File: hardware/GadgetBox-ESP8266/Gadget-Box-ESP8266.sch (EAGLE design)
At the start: 31 parts, among them U1 MCP73831T-2ACI/OT, U2 AP2112-3.3

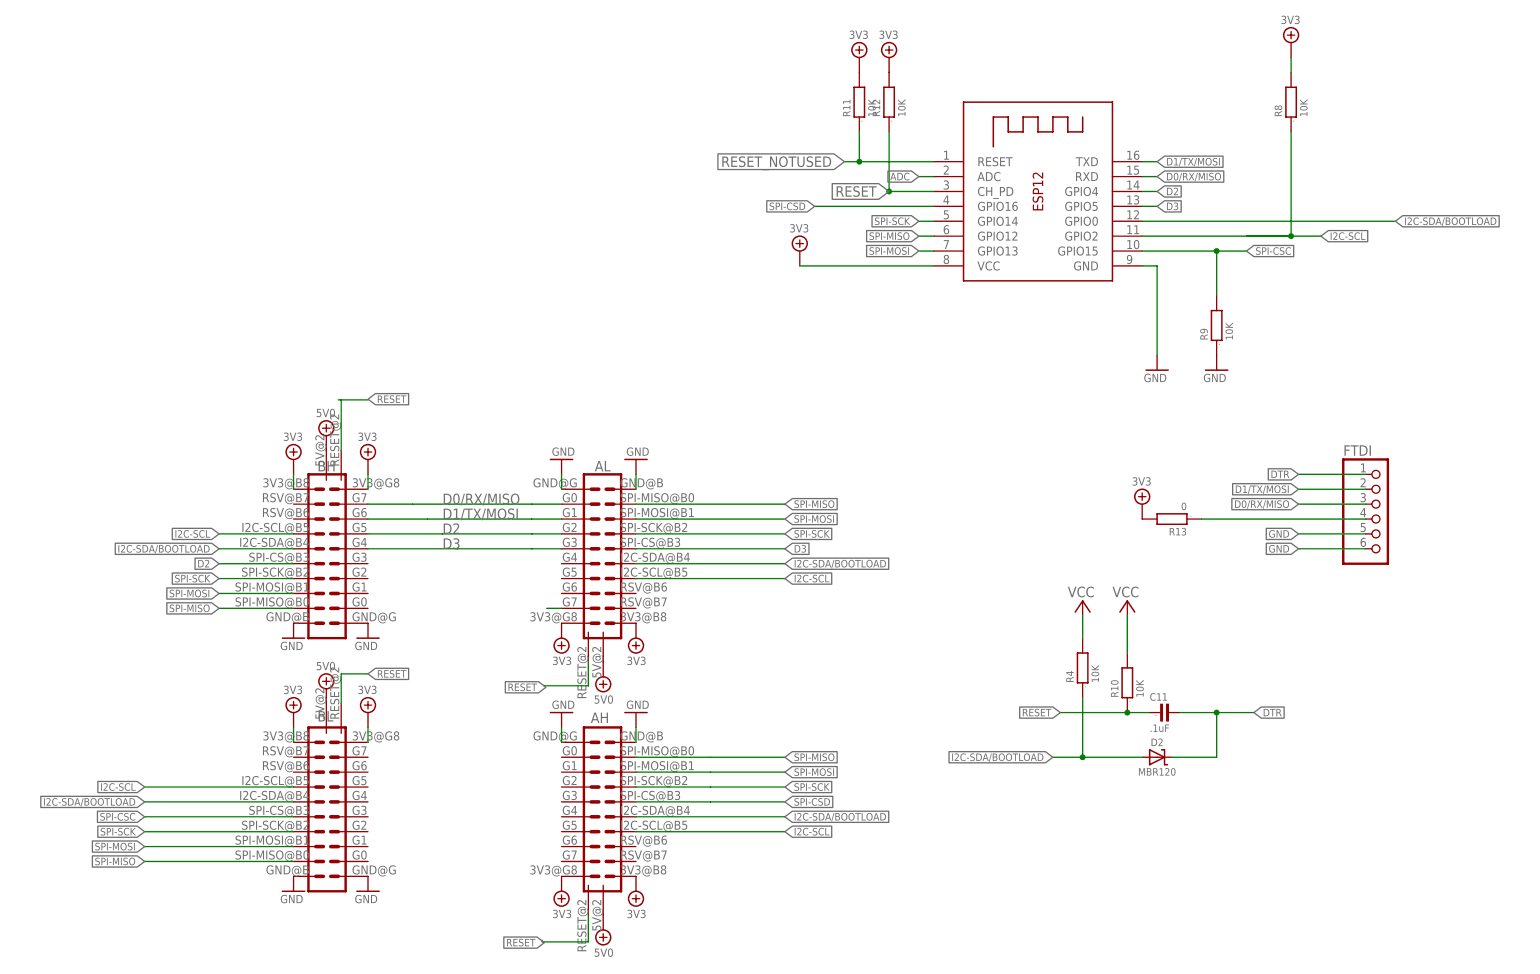
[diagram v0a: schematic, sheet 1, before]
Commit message: Removed Alt eCog headers and re-routed outside traces.
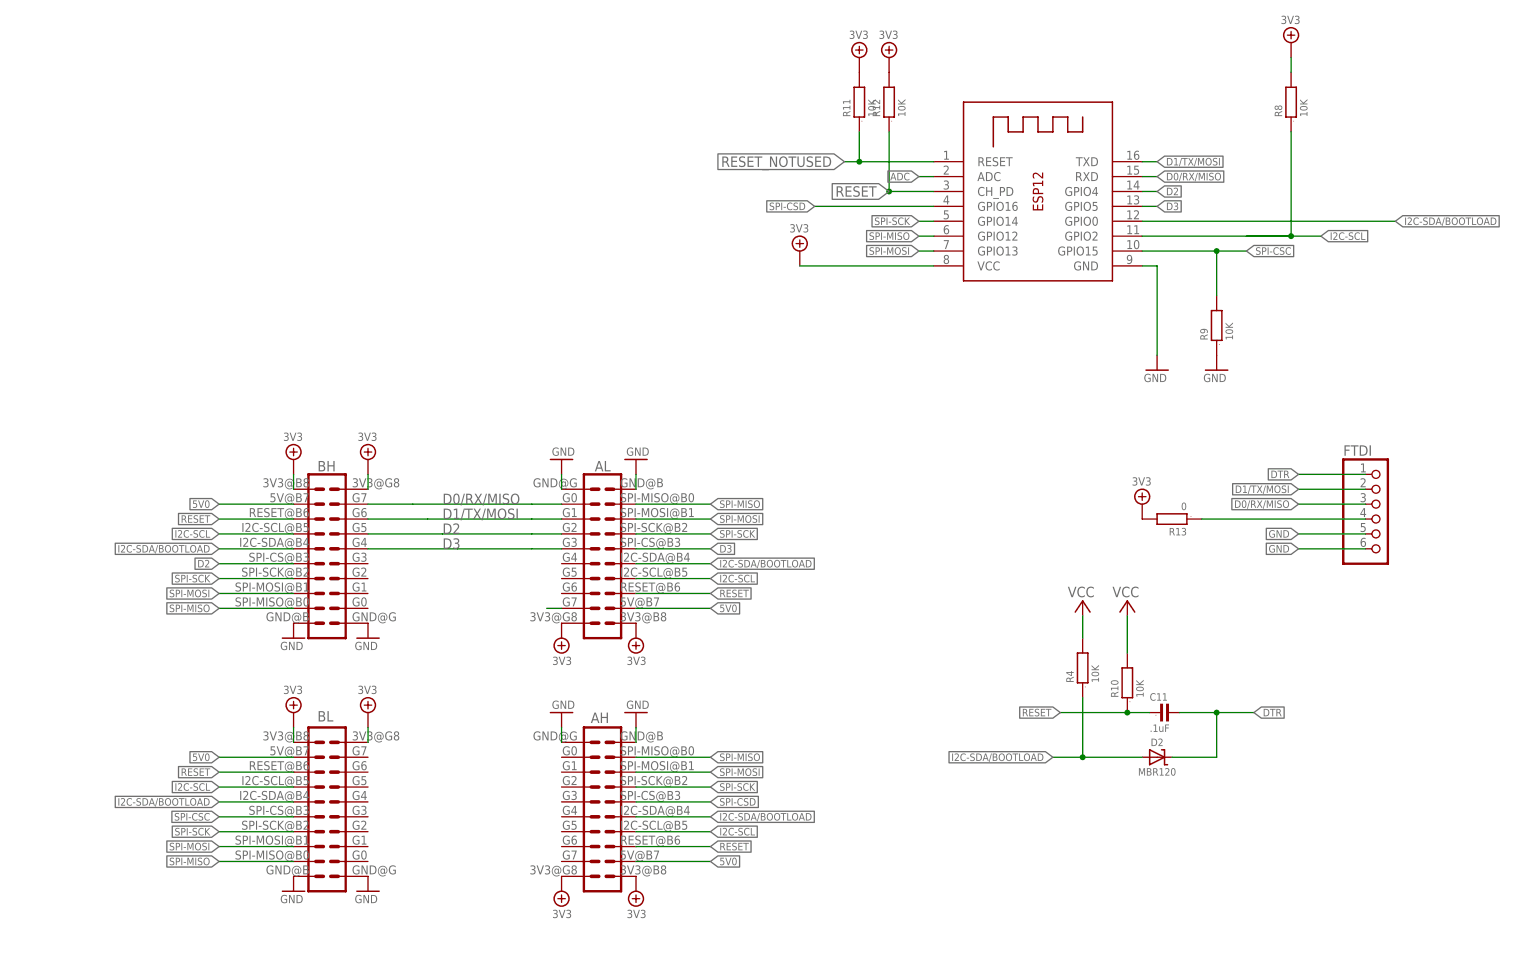
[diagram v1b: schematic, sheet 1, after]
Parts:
- AH, AL, BH, BL: value ECOGECOG_SLOT_ALT1 -> ECOGECOG_SLOT; device eCogs:ECOGECOG_SLOT_ALT1 -> eCogs:ECOGECOG_SLOT
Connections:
- net 5V0: now also AH.5V@B7, AL.5V@B7, BH.5V@B7, BL.5V@B7; no longer AH.5V@0, AL.5V@0, BH.5V@0, BL.5V@0
- net RESET: now also AH.RESET@B6, AL.RESET@B6, BH.RESET@B6, BL.RESET@B6; no longer AH.RESET@1, AL.RESET@1, BH.RESET@1, BL.RESET@1
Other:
- note added: "Attribution: The Battery Charging and Power portions of this schematic are from the Adafruit Huzzah Design."
- note removed: "Attribution: The Battery Charging and Power portions of this schemtic are from the Adafruit Huzzah Design."
